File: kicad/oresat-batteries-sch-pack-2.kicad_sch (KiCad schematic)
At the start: 79 parts, among them Q24 PM45VEN, Q25 PM45VEN, Q26 PM45VEN, Q27 PM45VEN, Q30 SI7625DN-T1-GE3, Q31 SI7625DN-T1-GE3, Q32 NTR4101, Q33 NTR4101, Q34 SI7625DN-T1-GE3, Q35 SI7625DN-T1-GE3, Q36 SI7625DN-T1-GE3, Q37 SI7625DN-T1-GE3, U13 S-8209AAA-T8T1U, U14 S-8209AAA-T8T1U, U15 LTC4412, U16 LTC4412, U17 MAX17205G

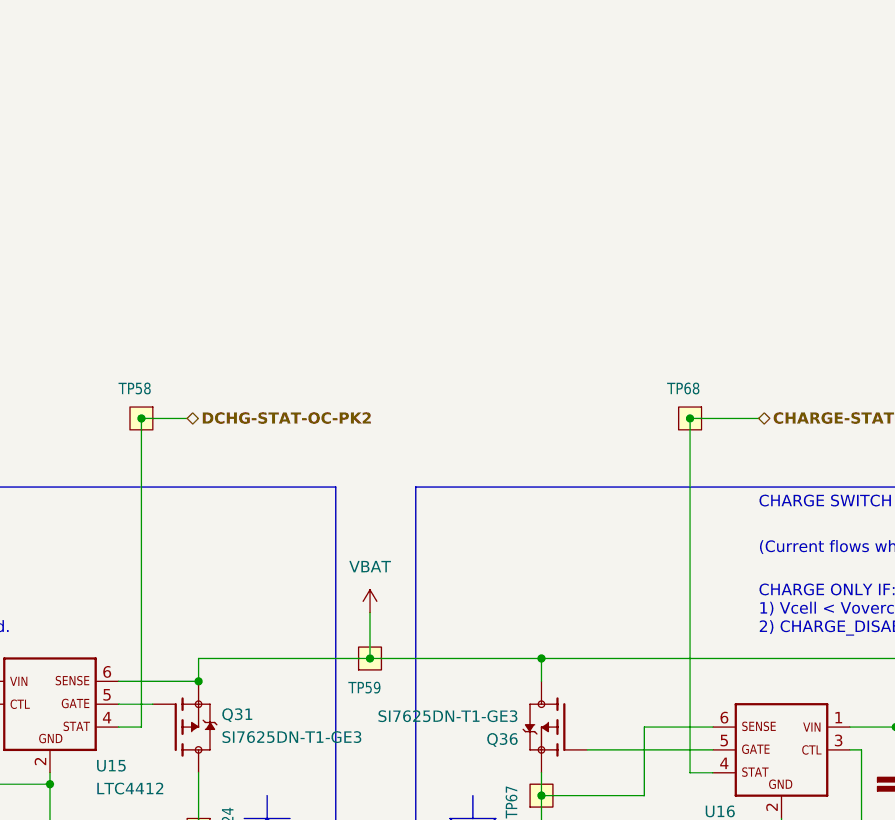
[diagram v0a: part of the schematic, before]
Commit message: Added +battery disconect mosfet and switch
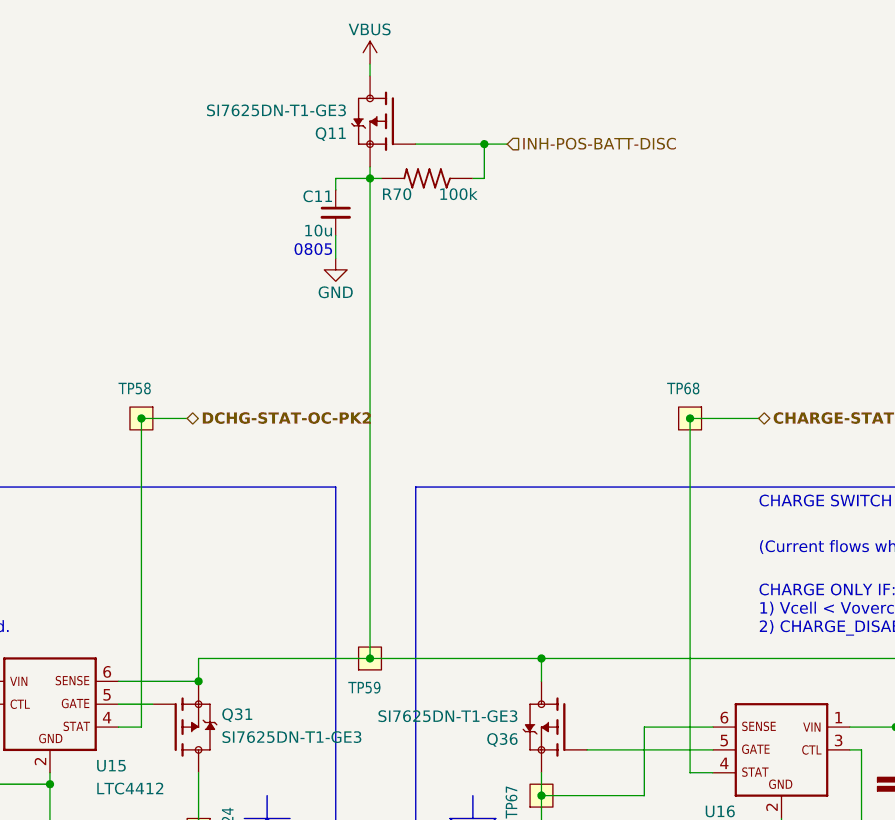
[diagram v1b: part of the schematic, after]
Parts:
- added C11: 10u, oresat-batteries:.0805-B-NOSILK, symbol Device:C_Small
- added Q11: SI7625DN-T1-GE3, oresat-batteries:POWERPAK-1212-8, symbol oresat-batteries-eagle-import:Q-VISHAY-MOSFET-PCH-POWERPAK-1212-8
- added R70: 100k, oresat-batteries:.0603-C-NOSILK, symbol oresat-batteries-eagle-import:R-US_0603-C-NOSILK
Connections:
- net GND: now also C11.2
- net VBAT: no longer names the net of C34.1, Q31.1 (S), Q31.2 (S), Q31.3 (S), Q36.5 (D), Q36.6 (D), Q36.7 (D), Q36.8 (D), Q36.PAD (D), TP59.1, U15.6 (SENSE), U16.1 (VIN)
- net VBAT: now also C11.1, Q11.1 (S), Q11.2 (S), Q11.3 (S), R70.2
- new net INH-POS-BATT-DISC: Q11.4 (G), R70.1
- new net VBUS: Q11.5 (D), Q11.6 (D), Q11.7 (D), Q11.8 (D), Q11.PAD (D)
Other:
- note added: "0805"

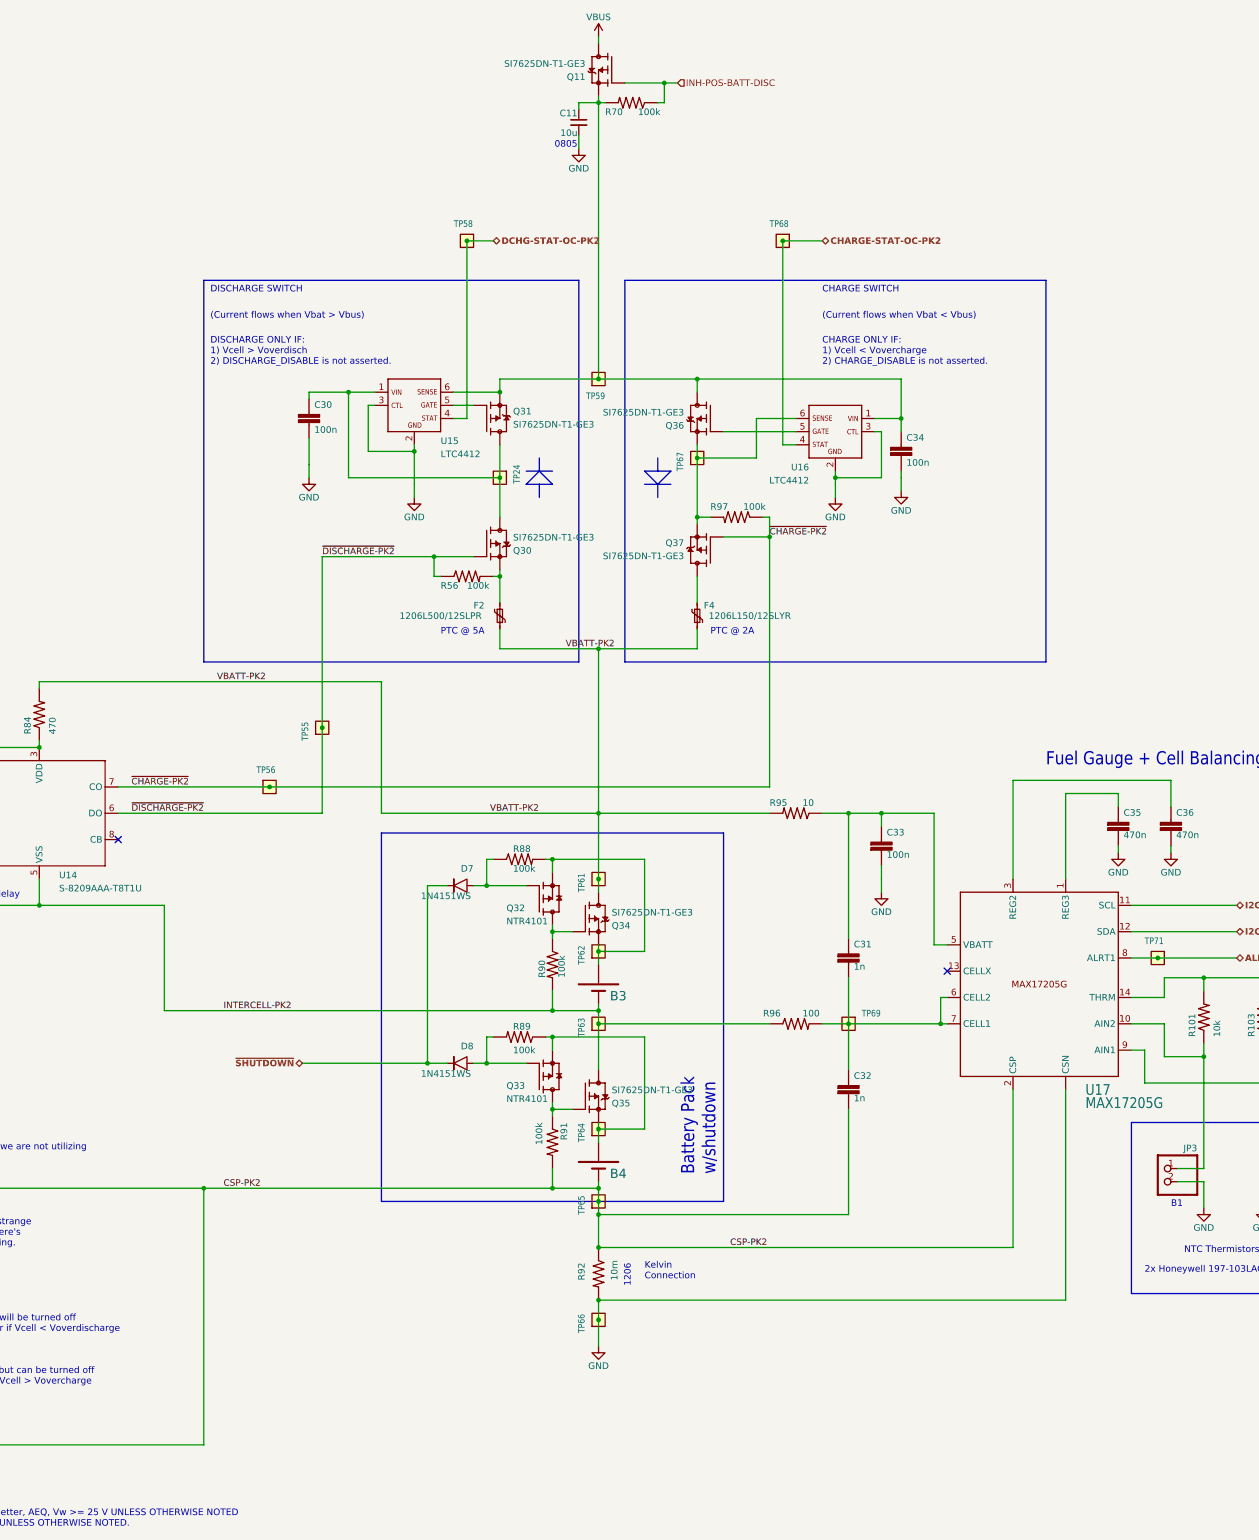
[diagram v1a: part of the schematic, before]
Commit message: Negative battery disconnects in. Ready for KiCad component upgrade.
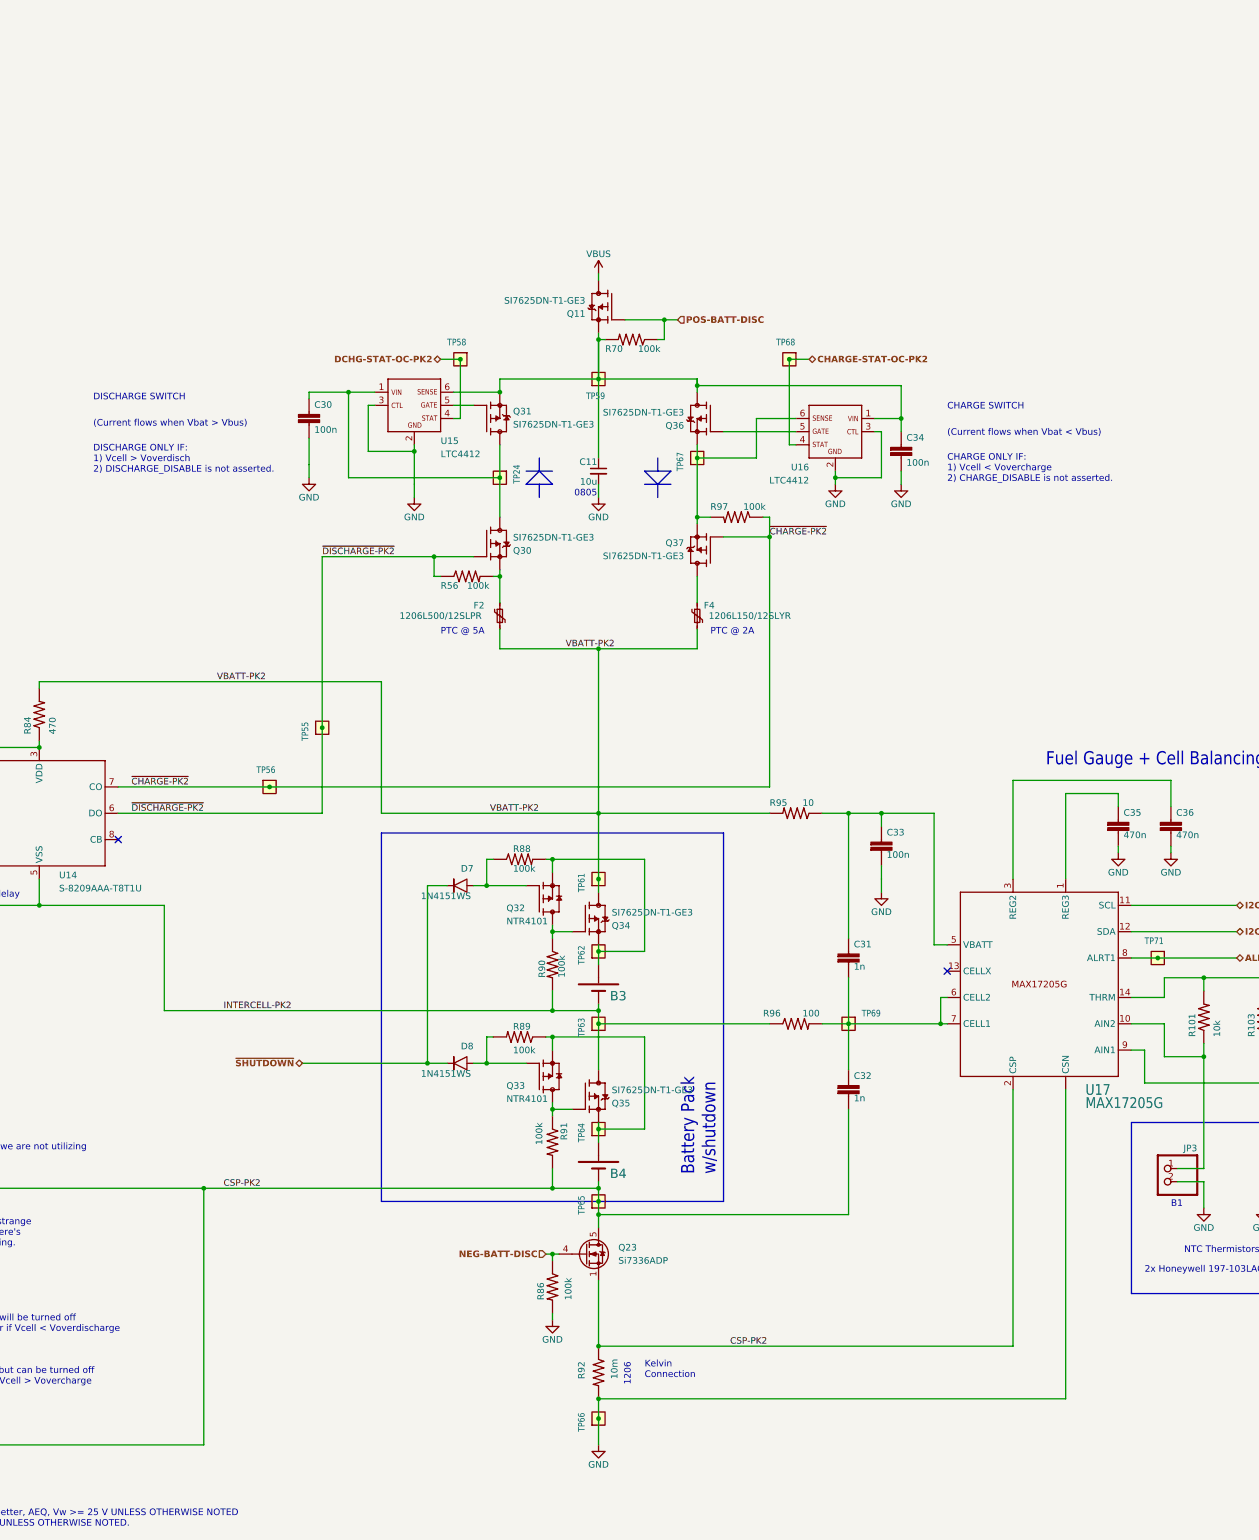
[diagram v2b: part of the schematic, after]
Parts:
- added Q23: Si7336ADP, Package_SO:PowerPAK_SO-8_Single, symbol Transistor_FET:Si7336ADP
- added R86: 100k, oresat-batteries:.0603-C-NOSILK, symbol oresat-batteries-eagle-import:R-US_0603-C-NOSILK
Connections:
- net CSP-PK2: now also Q23.1 (S), Q23.2 (S), Q23.3 (S), Q23.5 (D)
- net GND: now also R86.2
- net INH-POS-BATT-DISC renamed POS-BATT-DISC
- new net NEG-BATT-DISC: Q23.4 (G), R86.1
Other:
- moved on the sheet: C11, Q11, R70, R92, TP58, TP66, TP68

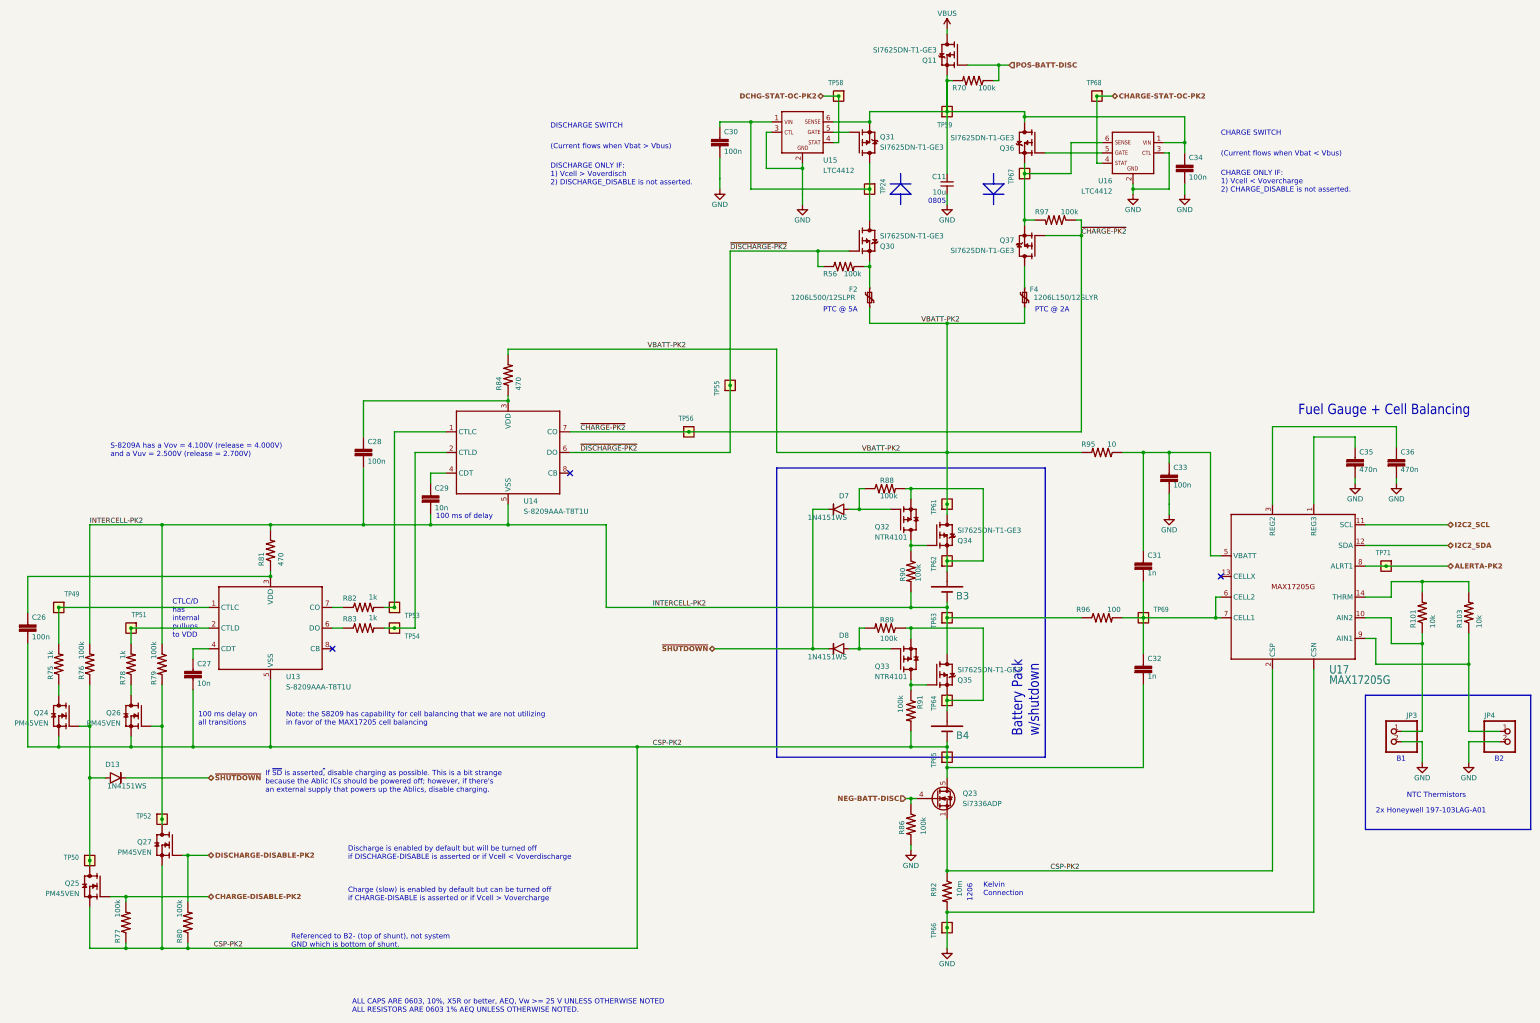
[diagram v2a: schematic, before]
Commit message: Renovated Schematic
Updated schematic symbols and made more uniform with changed resistor, capacitor, and FET symbols. Changed 0603 cap foot print to 0603 small in Oresat passives. Added 2 new resistors and 2 new caps in the power page. Removed old debug connector in favor of the new one. The changes made should make very little updates when pushing the changes to the PCB.
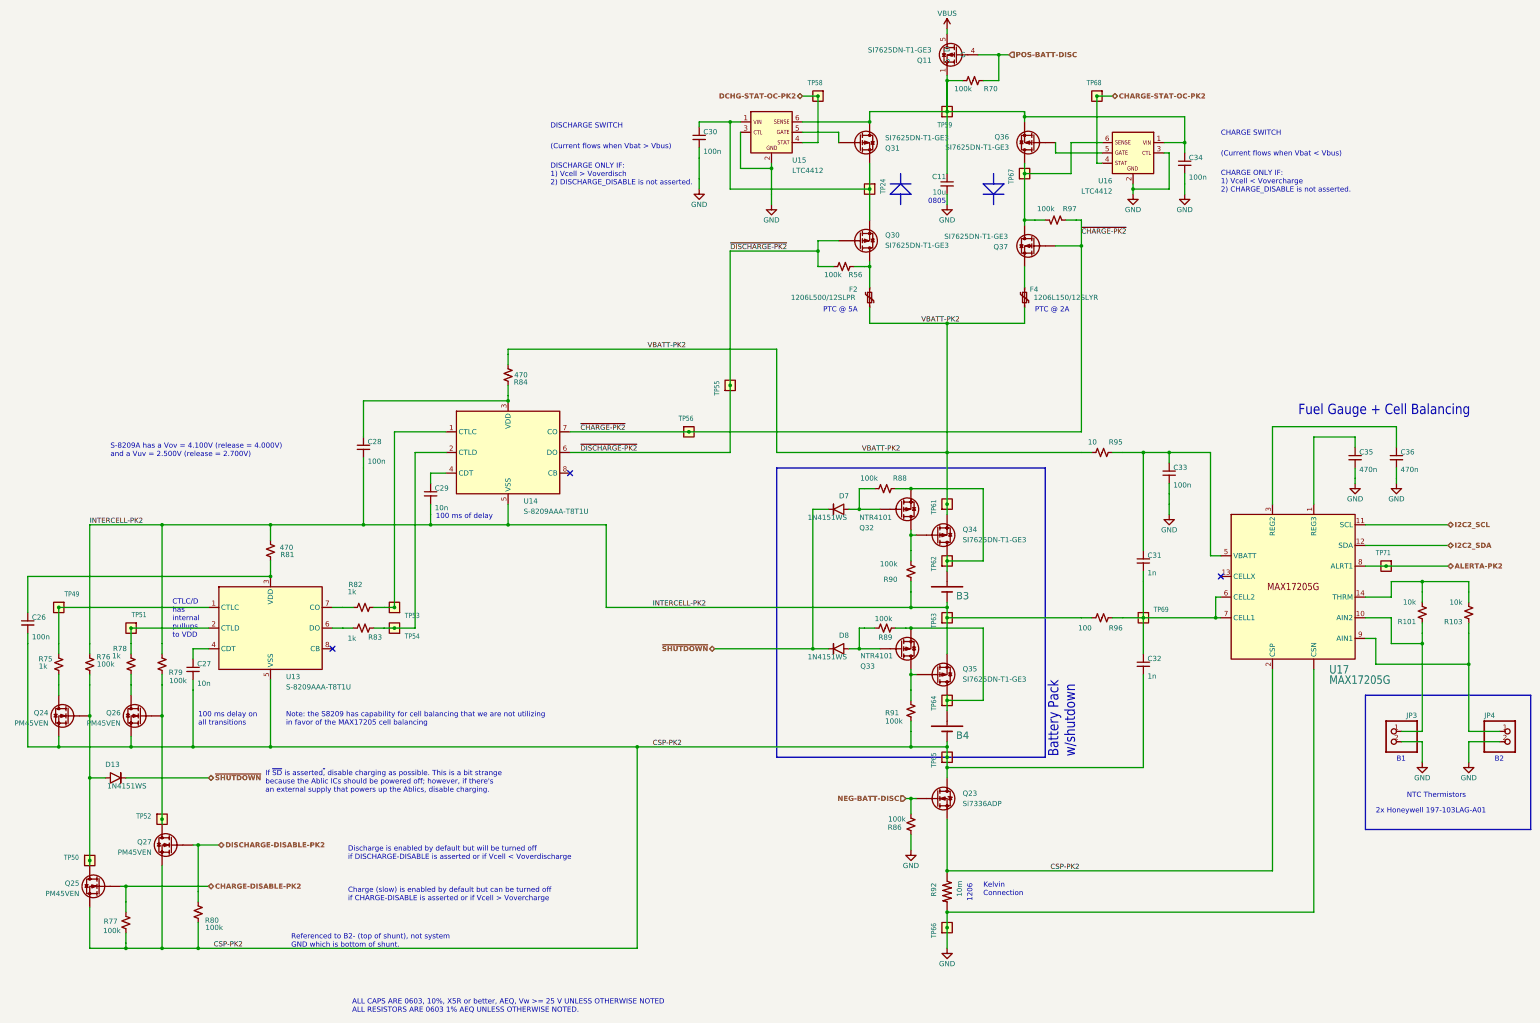
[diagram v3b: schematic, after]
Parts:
- C11: footprint oresat-batteries:.0805-B-NOSILK -> oresat-passives:0805-B-NOSILK
- C26, C27, C28, C29, C30, C31, C32, C33, C34, C35, C36: footprint oresat-batteries:.0603-C-NOSILK -> oresat-passives:c_0603-SMALL; symbol oresat-batteries-eagle-import:C-EU0603-C-NOSILK -> Device:C_Small
- Q24, Q25, Q26, Q27: symbol oresat-batteries-eagle-import:N-MOSFET-SOT-23-3 -> Transistor_FET:Q_NMOS_GSD
- Q32, Q33: symbol oresat-batteries-eagle-import:P-MOSFET-SOT23-3 -> Transistor_FET:Q_PMOS_GSD
- R101, R103, R56, R70, R75, R76, R77, R78, R79, R80, R81, R82, R83, R84, R86, R88, R89, R90, R91, R95, R96, R97: symbol oresat-batteries-eagle-import:R-US_0603-C-NOSILK -> Device:R_Small_US
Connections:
- net INTERCELL-PK2: now also Q35.1 (S); no longer Q35.5 (D), Q35.6 (D), Q35.7 (D), Q35.8 (D), Q35.PAD (D)
- net VBATT-PK2: now also Q34.1 (S); no longer Q34.5 (D), Q34.6 (D), Q34.7 (D), Q34.8 (D), Q34.PAD (D)
- net VBUS: no longer Q11.6 (D), Q11.7 (D), Q11.8 (D), Q11.PAD (D)
- net ~{CHARGE-PK2}: now also R97.2; no longer R97.1
- net at B3.1 (POS), Q32.2 (S), R88.2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: now also Q34.5 (D); no longer Q34.1 (S), Q34.2 (S), Q34.3 (S)
- net at B4.1 (POS), Q33.2 (S), R89.1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: now also Q35.5 (D); no longer Q35.1 (S), Q35.2 (S), Q35.3 (S)
- new net: C11.1, C34.1, Q11.1 (S), Q31.5 (D), Q36.1 (S), R70.2, TP59.1, U15.6 (SENSE), U16.1 (VIN)
- new net: F2.1, Q30.5 (D), R56.2
- new net: C30.1, Q30.1 (S), Q31.1 (S), TP24.1, U15.1 (VIN)
- new net: Q36.5 (D), Q37.5 (D), R97.1, TP67.1, U16.6 (SENSE)
- new net: F4.1, Q37.1 (S)
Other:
- moved on the sheet: TP58
